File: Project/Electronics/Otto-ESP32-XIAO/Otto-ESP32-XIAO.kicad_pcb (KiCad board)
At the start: 2 copper layers, 60 x 52 mm, 70 parts, among them J1 Conn_01x03, J10 Conn_01x02, J11 Conn_01x04, J12 OLED 0,91" - I2C (SKU21796), J13 MPU6050, J2 Conn_01x03, J3 Conn_01x03, J4 Conn_01x03, J5 Conn_01x03, J6 Conn_01x03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

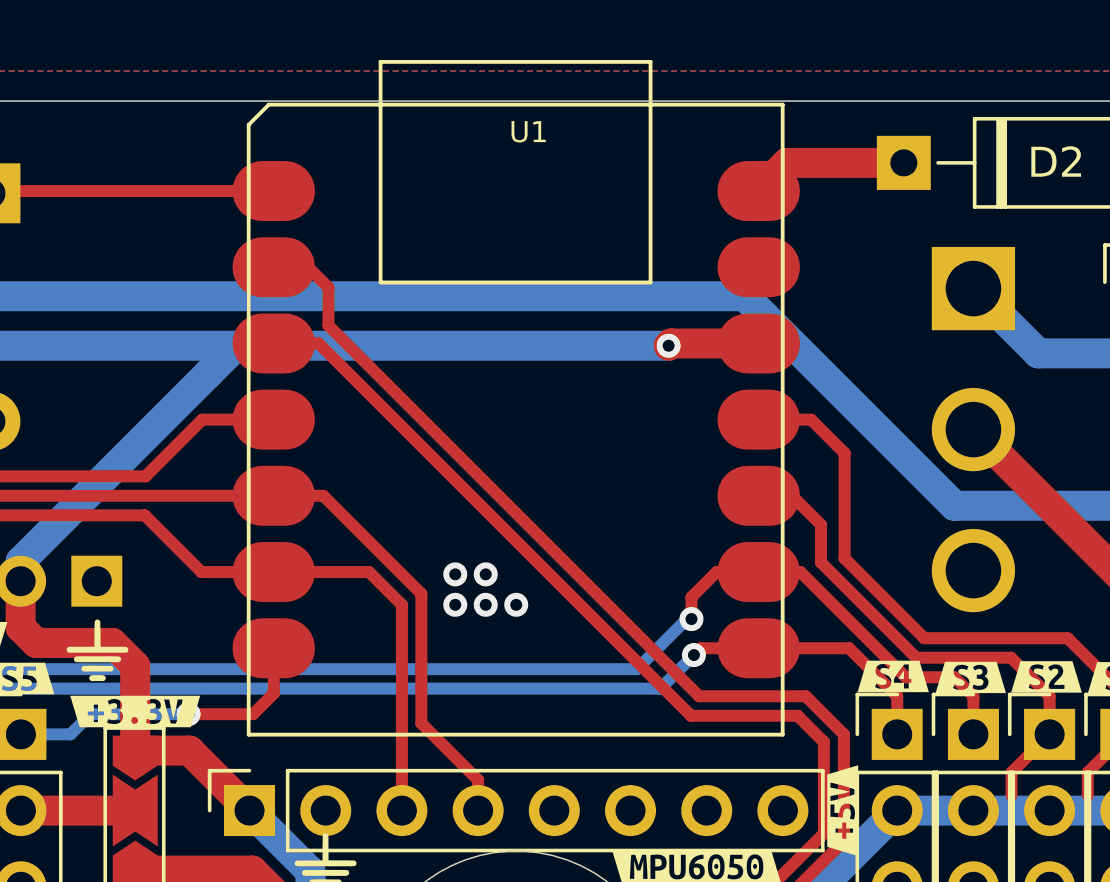
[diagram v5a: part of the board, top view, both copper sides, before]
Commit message: enlarge pins on C3 socket
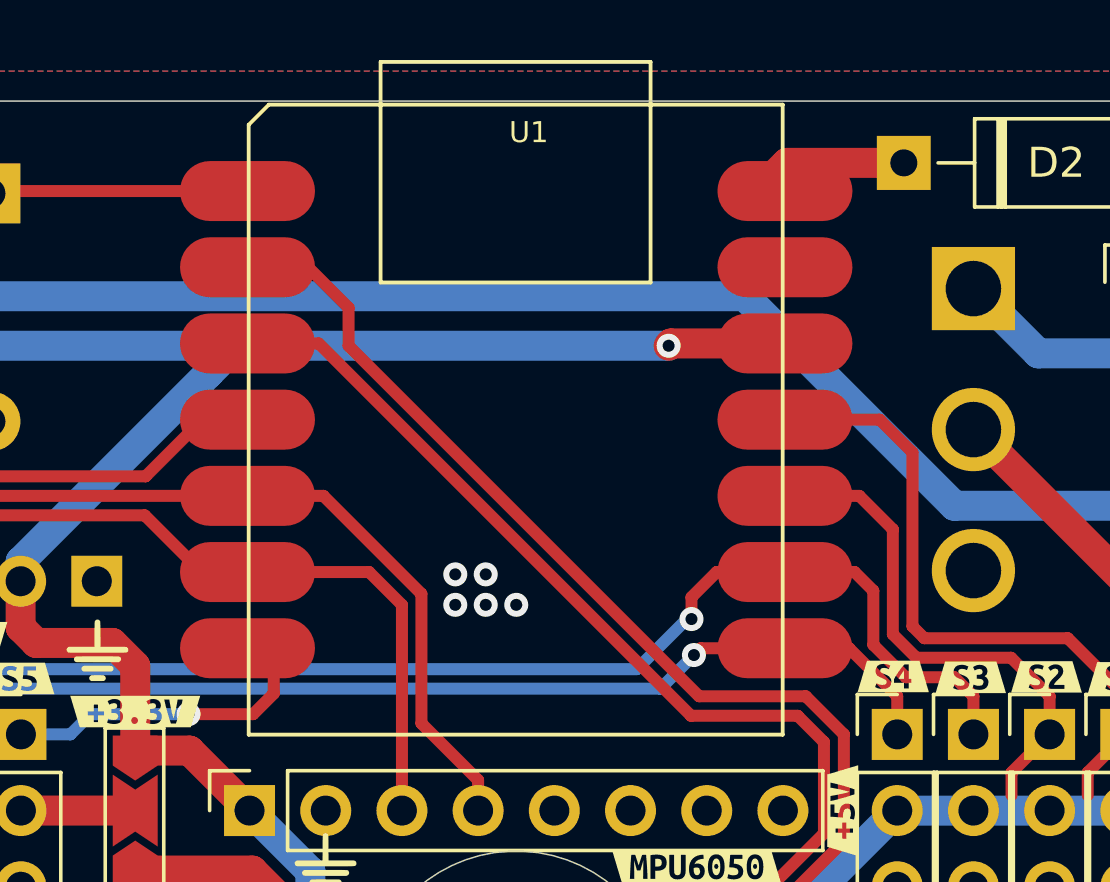
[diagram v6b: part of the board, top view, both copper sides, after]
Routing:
- net Servo-1: track 36.9 -> 38.2 mm
- net Servo-2: track 31.7 -> 33.0 mm
- net Servo-3: track 55.8 -> 56.8 mm
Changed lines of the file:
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@@
 		(pad "1" smd roundrect
 			(at 0.835 -18.12)
-			(size 2.75 2)
+			(size 4.5 2)
+			(drill
+				(offset -0.875 0)
+			)
 			(layers "F.Cu" "F.Paste" "F.Mask")
 			(roundrect_rratio 0.5)
@@
 		(pad "2" smd roundrect
 			(at 0.835 -15.58)
-			(size 2.75 2)
+			(size 4.5 2)
+			(drill
+				(offset -0.875 0)
+			)
 			(layers "F.Cu" "F.Paste" "F.Mask")
 			(roundrect_rratio 0.5)
@@
 		(pad "3" smd roundrect
 			(at 0.835 -13.04)
-			(size 2.75 2)
+			(size 4.5 2)
+			(drill
+				(offset -0.875 0)
+			)
 			(layers "F.Cu" "F.Paste" "F.Mask")
 			(roundrect_rratio 0.5)
@@
 		(pad "4" smd roundrect
 			(at 0.835 -10.5)
-			(size 2.75 2)
+			(size 4.5 2)
+			(drill
+				(offset -0.875 0)
+			)
 			(layers "F.Cu" "F.Paste" "F.Mask")
 			(roundrect_rratio 0.5)
@@
 		(pad "5" smd roundrect
 			(at 0.835 -7.96)
-			(size 2.75 2)
+			(size 4.5 2)
+			(drill
+				(offset -0.875 0)
+			)
 			(layers "F.Cu" "F.Paste" "F.Mask")
 			(roundrect_rratio 0.5)
@@
 		(pad "6" smd roundrect
 			(at 0.835 -5.42)
-			(size 2.75 2)
+			(size 4.5 2)
+			(drill
+				(offset -0.875 0)
+			)
 			(layers "F.Cu" "F.Paste" "F.Mask")
 			(roundrect_rratio 0.5)
@@
 		(pad "7" smd roundrect
 			(at 0.835 -2.88)
-			(size 2.75 2)
+			(size 4.5 2)
+			(drill
+				(offset -0.875 0)
+			)
 			(layers "F.Cu" "F.Paste" "F.Mask")
 			(roundrect_rratio 0.5)
@@
 		(pad "8" smd roundrect
 			(at 17 -2.88)
-			(size 2.75 2)
+			(size 4.5 2)
+			(drill
+				(offset 0.875 0)
+			)
 			(layers "F.Cu" "F.Paste" "F.Mask")
 			(roundrect_rratio 0.5)
@@
 		(pad "9" smd roundrect
 			(at 17 -5.42)
-			(size 2.75 2)
+			(size 4.5 2)
+			(drill
+				(offset 0.875 0)
+			)
 			(layers "F.Cu" "F.Paste" "F.Mask")
 			(roundrect_rratio 0.5)
@@
 		(pad "10" smd roundrect
 			(at 17 -7.96)
-			(size 2.75 2)
+			(size 4.5 2)
+			(drill
+				(offset 0.875 0)
+			)
 			(layers "F.Cu" "F.Paste" "F.Mask")
 			(roundrect_rratio 0.5)
@@
 		(pad "11" smd roundrect
 			(at 17 -10.5)
-			(size 2.75 2)
+			(size 4.5 2)
+			(drill
+				(offset 0.875 0)
+			)
 			(layers "F.Cu" "F.Paste" "F.Mask")
 			(roundrect_rratio 0.5)
@@
 		(pad "12" smd roundrect
 			(at 17 -13.04)
-			(size 2.75 2)
+			(size 4.5 2)
+			(drill
+				(offset 0.875 0)
+			)
 			(layers "F.Cu" "F.Paste" "F.Mask")
 			(roundrect_rratio 0.5)
@@
 		(pad "13" smd roundrect
 			(at 17 -15.58)
-			(size 2.75 2)
+			(size 4.5 2)
+			(drill
+				(offset 0.875 0)
+			)
 			(layers "F.Cu" "F.Paste" "F.Mask")
 			(roundrect_rratio 0.5)
@@
 		(pad "14" smd roundrect
 			(at 17 -18.12)
-			(size 2.75 2)
+			(size 4.5 2)
+			(drill
+				(offset 0.875 0)
+			)
 			(layers "F.Cu" "F.Paste" "F.Mask")
 			(roundrect_rratio 0.5)
@@
 	)
 	(segment
-		(start 149.05 73.142)
-		(end 149.05 76.952)
-		(width 0.2)
-		(layer "F.Cu")
-		(net 5)
-	)
-	(segment
-		(start 139.82925 60.61925)
-		(end 138.0825 60.61925)
+		(start 143.208 67.508762)
+		(end 143.208 61.712)
 		(width 0.4)
 		(layer "F.Cu")
@@
 	)
 	(segment
-		(start 140.944619 61.734619)
-		(end 139.82925 60.61925)
-		(width 0.4)
+		(start 149.05 73.142)
+		(end 149.05 76.952)
+		(width 0.2)
 		(layer "F.Cu")
 		(net 5)
@@
 	)
 	(segment
-		(start 141.43 81.27)
-		(end 141.43 80)
+		(start 150.32 71.11)
+		(end 150.32 69.84)
 		(width 0.4)
 		(layer "F.Cu")
@@
 	)
 	(segment
-		(start 148.385 67.905)
-		(end 143.604238 67.905)
+		(start 141.43 81.27)
+		(end 141.43 80)
 		(width 0.4)
 		(layer "F.Cu")
@@
 	(segment
 		(start 143.604238 67.905)
-		(end 140.944619 65.245381)
+		(end 143.208 67.508762)
 		(width 0.4)
 		(layer "F.Cu")
@@
 	)
 	(segment
-		(start 140.944619 65.245381)
-		(end 140.944619 61.734619)
+		(start 148.385 67.905)
+		(end 143.604238 67.905)
 		(width 0.4)
 		(layer "F.Cu")
@@
 	)
 	(segment
-		(start 150.32 71.11)
-		(end 150.32 69.84)
+		(start 143.208 61.712)
+		(end 142.11525 60.61925)
 		(width 0.4)
 		(layer "F.Cu")
@@
 	)
 	(segment
+		(start 150.32 69.84)
+		(end 148.385 67.905)
+		(width 0.4)
+		(layer "F.Cu")
+		(net 5)
+	)
+	(segment
 		(start 148.288 78.984)
 		(end 149.05 78.222)
@@
 	)
 	(segment
-		(start 150.32 69.84)
-		(end 148.385 67.905)
+		(start 142.11525 60.61925)
+		(end 138.0825 60.61925)
 		(width 0.4)
 		(layer "F.Cu")
@@
 	)
 	(segment
-		(start 143.335 68.555)
-		(end 140.16 65.38)
+		(start 146.495 68.555)
+		(end 143.335 68.555)
 		(width 0.4)
 		(layer "F.Cu")
@@
 	)
 	(segment
-		(start 140.16 65.38)
-		(end 140.16 64.125)
+		(start 146.51 73.142)
+		(end 146.51 72.38)
 		(width 0.4)
 		(layer "F.Cu")
@@
 	)
 	(segment
-		(start 146.51 73.142)
-		(end 146.51 72.38)
+		(start 147.78 71.11)
+		(end 147.78 69.84)
 		(width 0.4)
 		(layer "F.Cu")
@@
 	)
 	(segment
-		(start 145.89 78.334)
-		(end 146.51 77.714)
+		(start 141.437083 63.15925)
+		(end 138.0825 63.15925)
 		(width 0.4)
 		(layer "F.Cu")
@@
 	)
 	(segment
-		(start 146.51 77.714)
-		(end 146.51 76.952)
+		(start 142.554023 64.27619)
+		(end 141.437083 63.15925)
 		(width 0.4)
 		(layer "F.Cu")
@@
 	)
 	(segment
-		(start 146.51 72.38)
-		(end 147.78 71.11)
+		(start 145.89 78.334)
+		(end 146.51 77.714)
 		(width 0.4)
 		(layer "F.Cu")
@@
 	)
 	(segment
-		(start 147.54 71.11)
-		(end 147.78 71.11)
+		(start 142.554023 67.774023)
+		(end 142.554023 64.27619)
 		(width 0.4)
 		(layer "F.Cu")
@@
 	)
 	(segment
-		(start 146.495 68.555)
-		(end 143.335 68.555)
+		(start 146.51 77.714)
+		(end 146.51 76.952)
 		(width 0.4)
 		(layer "F.Cu")
@@
 	)
 	(segment
-		(start 138.89 80)
-		(end 140.556 78.334)
+		(start 146.51 72.38)
+		(end 147.78 71.11)
 		(width 0.4)
 		(layer "F.Cu")
@@
 	)
 	(segment
-		(start 147.78 71.11)
-		(end 147.78 69.84)
+		(start 143.335 68.555)
+		(end 142.554023 67.774023)
 		(width 0.4)
 		(layer "F.Cu")
@@
 	)
 	(segment
-		(start 139.19425 63.15925)
-		(end 138.0825 63.15925)
+		(start 147.54 71.11)
+		(end 147.78 71.11)
 		(width 0.4)
 		(layer "F.Cu")
@@
 	)
 	(segment
-		(start 140.16 64.125)
-		(end 139.19425 63.15925)
+		(start 138.89 80)
+		(end 140.556 78.334)
 		(width 0.4)
 		(layer "F.Cu")
@@
 	)
 	(segment
-		(start 138.0825 65.69925)
-		(end 139.478488 65.69925)
+		(start 142.984238 69.205)
+		(end 144.605 69.205)
 		(width 0.4)
 		(layer "F.Cu")
@@
 	)
 	(segment
-		(start 144.605 69.205)
-		(end 145.24 69.84)
+		(start 141.27943 65.69925)
+		(end 141.904023 66.323843)
 		(width 0.4)
 		(layer "F.Cu")
@@
 	)
 	(segment
+		(start 141.904023 66.323843)
+		(end 141.904023 68.124785)
+		(width 0.4)
+		(layer "F.Cu")
+		(net 7)
+	)
+	(segment
+		(start 141.904023 68.124785)
+		(end 142.984238 69.205)
+		(width 0.4)
+		(layer "F.Cu")
+		(net 7)
+	)
+	(segment
 		(start 135.842 66.538)
 		(end 136.68075 65.69925)
@@
 	)
 	(segment
-		(start 139.478488 65.69925)
-		(end 142.984238 69.205)
+		(start 144.605 69.205)
+		(end 145.24 69.84)
 		(width 0.4)
 		(layer "F.Cu")
@@
 	)
 	(segment
-		(start 142.984238 69.205)
-		(end 144.605 69.205)
+		(start 138.0825 65.69925)
+		(end 141.27943 65.69925)
 		(width 0.4)
 		(layer "F.Cu")
@@
 	)
 	(segment
-		(start 137.62 77.968)
-		(end 140.922 74.666)
+		(start 136.096 69.84)
+		(end 124.412 58.156)
 		(width 0.4)
 		(layer "F.Cu")
@@
 	)
 	(segment
-		(start 139.652 69.84)
-		(end 136.096 69.84)
+		(start 123.06525 55.53925)
+		(end 121.9175 55.53925)
 		(width 0.4)
 		(layer "F.Cu")
@@
 	)
 	(segment
-		(start 136.096 69.84)
-		(end 123.7425 57.4865)
+		(start 137.62 77.968)
+		(end 140.922 74.666)
 		(width 0.4)
 		(layer "F.Cu")
@@
 	)
 	(segment
-		(start 137.62 91.176)
-		(end 137.62 77.968)
+		(start 140.922 74.666)
+		(end 140.922 71.11)
 		(width 0.4)
 		(layer "F.Cu")
@@
 	)
 	(segment
-		(start 140.922 74.666)
-		(end 140.922 71.11)
+		(start 124.412 56.886)
+		(end 123.06525 55.53925)
 		(width 0.4)
 		(layer "F.Cu")
@@
 	)
 	(segment
-		(start 140.922 71.11)
-		(end 139.652 69.84)
+		(start 124.412 58.156)
+		(end 124.412 56.886)
 		(width 0.4)
 		(layer "F.Cu")
@@
 	)
 	(segment
-		(start 123.06525 55.53925)
-		(end 121.9175 55.53925)
+		(start 139.652 69.84)
+		(end 136.096 69.84)
 		(width 0.4)
 		(layer "F.Cu")
@@
 	)
 	(segment
-		(start 123.7425 56.2165)
-		(end 123.06525 55.53925)
+		(start 140.922 71.11)
+		(end 139.652 69.84)
 		(width 0.4)
 		(layer "F.Cu")
@@
 	)
 	(segment
-		(start 123.7425 57.4865)
-		(end 123.7425 56.2165)
+		(start 137.62 91.176)
+		(end 137.62 77.968)
 		(width 0.4)
 		(layer "F.Cu")

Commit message: New PCB lite version
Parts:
- added C3: C_Small, Capacitor_THT:C_Disc_D6.0mm_W2.5mm_P5.00mm, F.Cu at (163.6, 50.5)
- added C4: C_Small, Capacitor_THT:C_Disc_D6.0mm_W2.5mm_P5.00mm, F.Cu at (163.1, 62.7)
